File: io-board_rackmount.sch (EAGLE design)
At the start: 25 parts

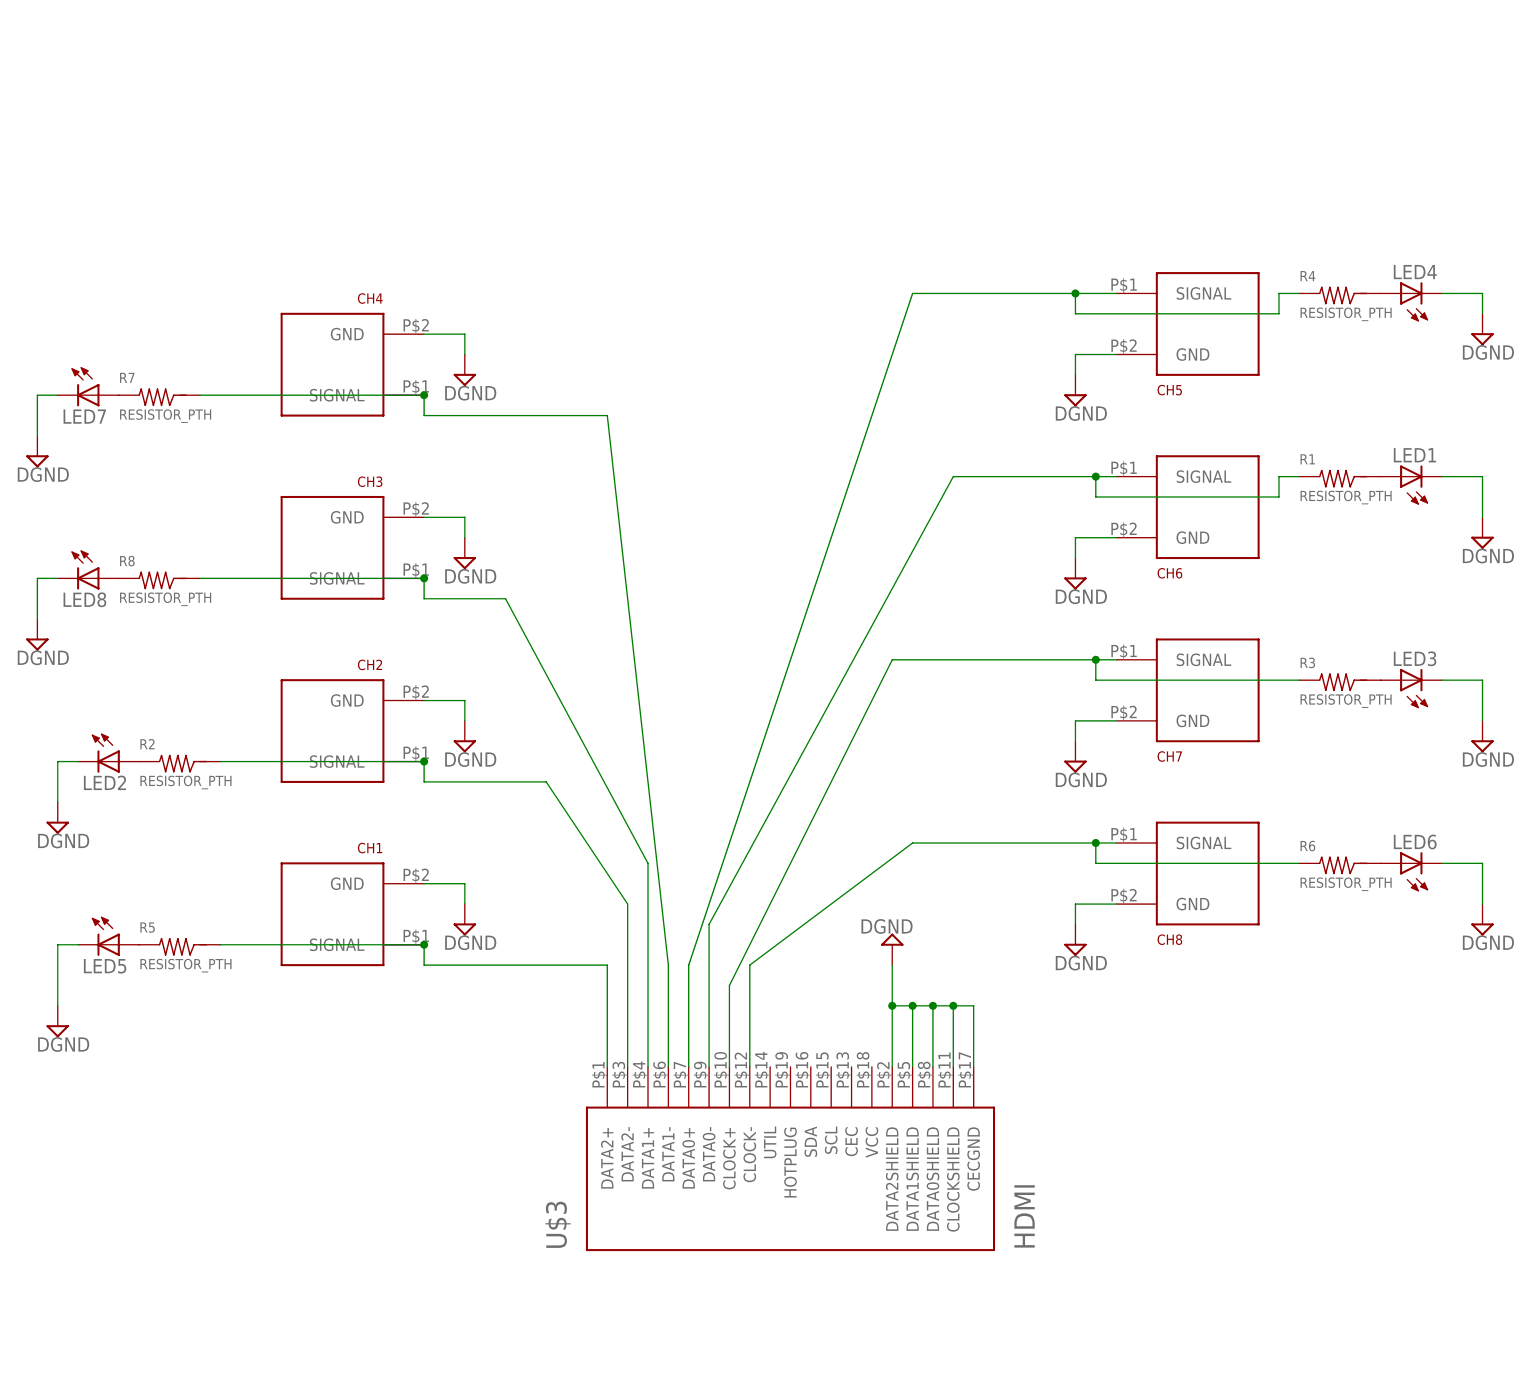
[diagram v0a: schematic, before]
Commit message: changed rackmounted IO board to single 8ch board
to be used with laser-cut mounting panel, or on its own
added pin headers for i2c and channels
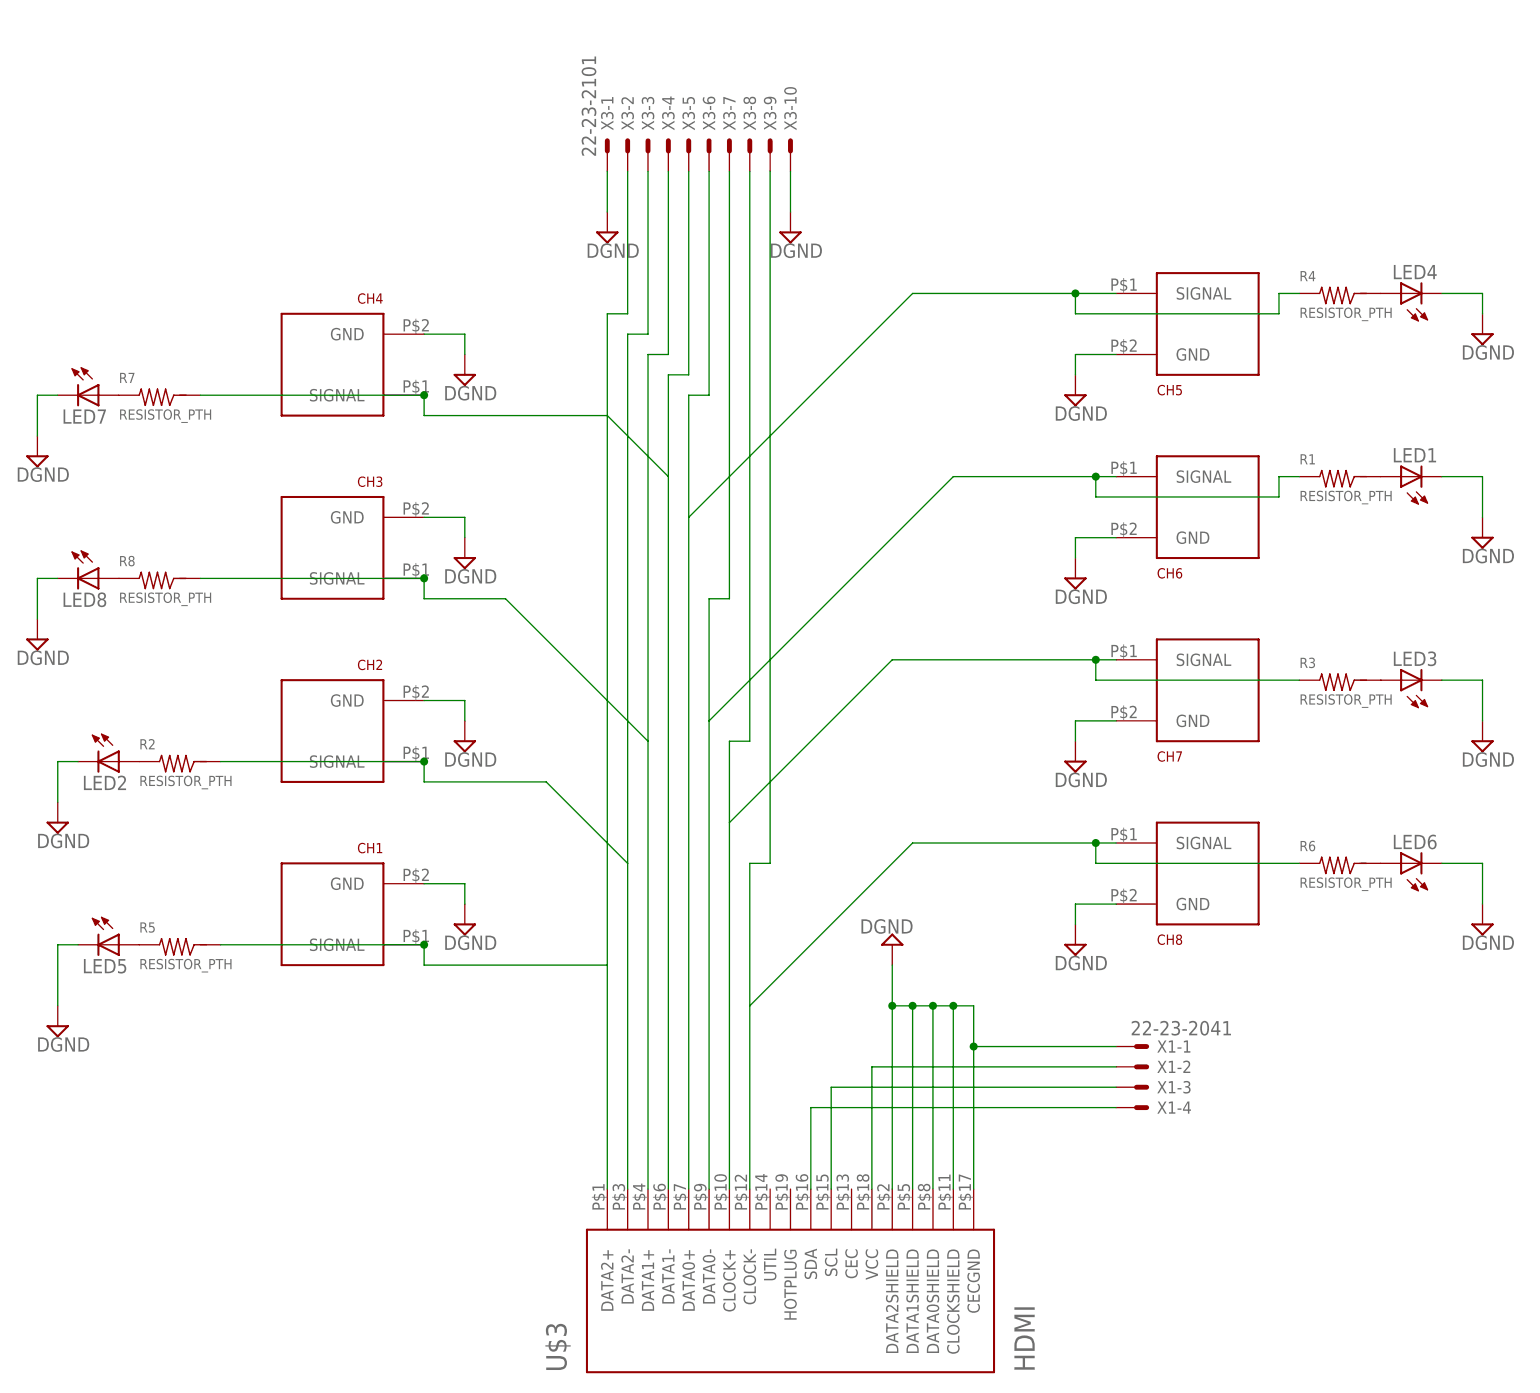
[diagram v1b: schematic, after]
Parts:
- added X1: 22-23-2041, con-molex:22-23-2041
- added X3: 22-23-2101, con-molex:22-23-2101
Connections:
- new net I2C_CLK: U$3.SCL, X1-3.S
- new net I2C_DAT: U$3.SDA, X1-4.S
- new net VCC: U$3.VCC, X1-2.S
- net CH6: now also X3-7.S
- net DGND: now also X1-1.S, X3-1.S, X3-10.S
- net N$2: now also X3-4.S
- net N$23: now also X3-5.S
- net N$3: now also X3-3.S
- net N$4: now also X3-2.S
- net N$5: now also X3-6.S
- net N$7: now also X3-8.S
- net N$8: now also X3-9.S
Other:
- moved on the sheet: U$3

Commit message: Remove LEDs
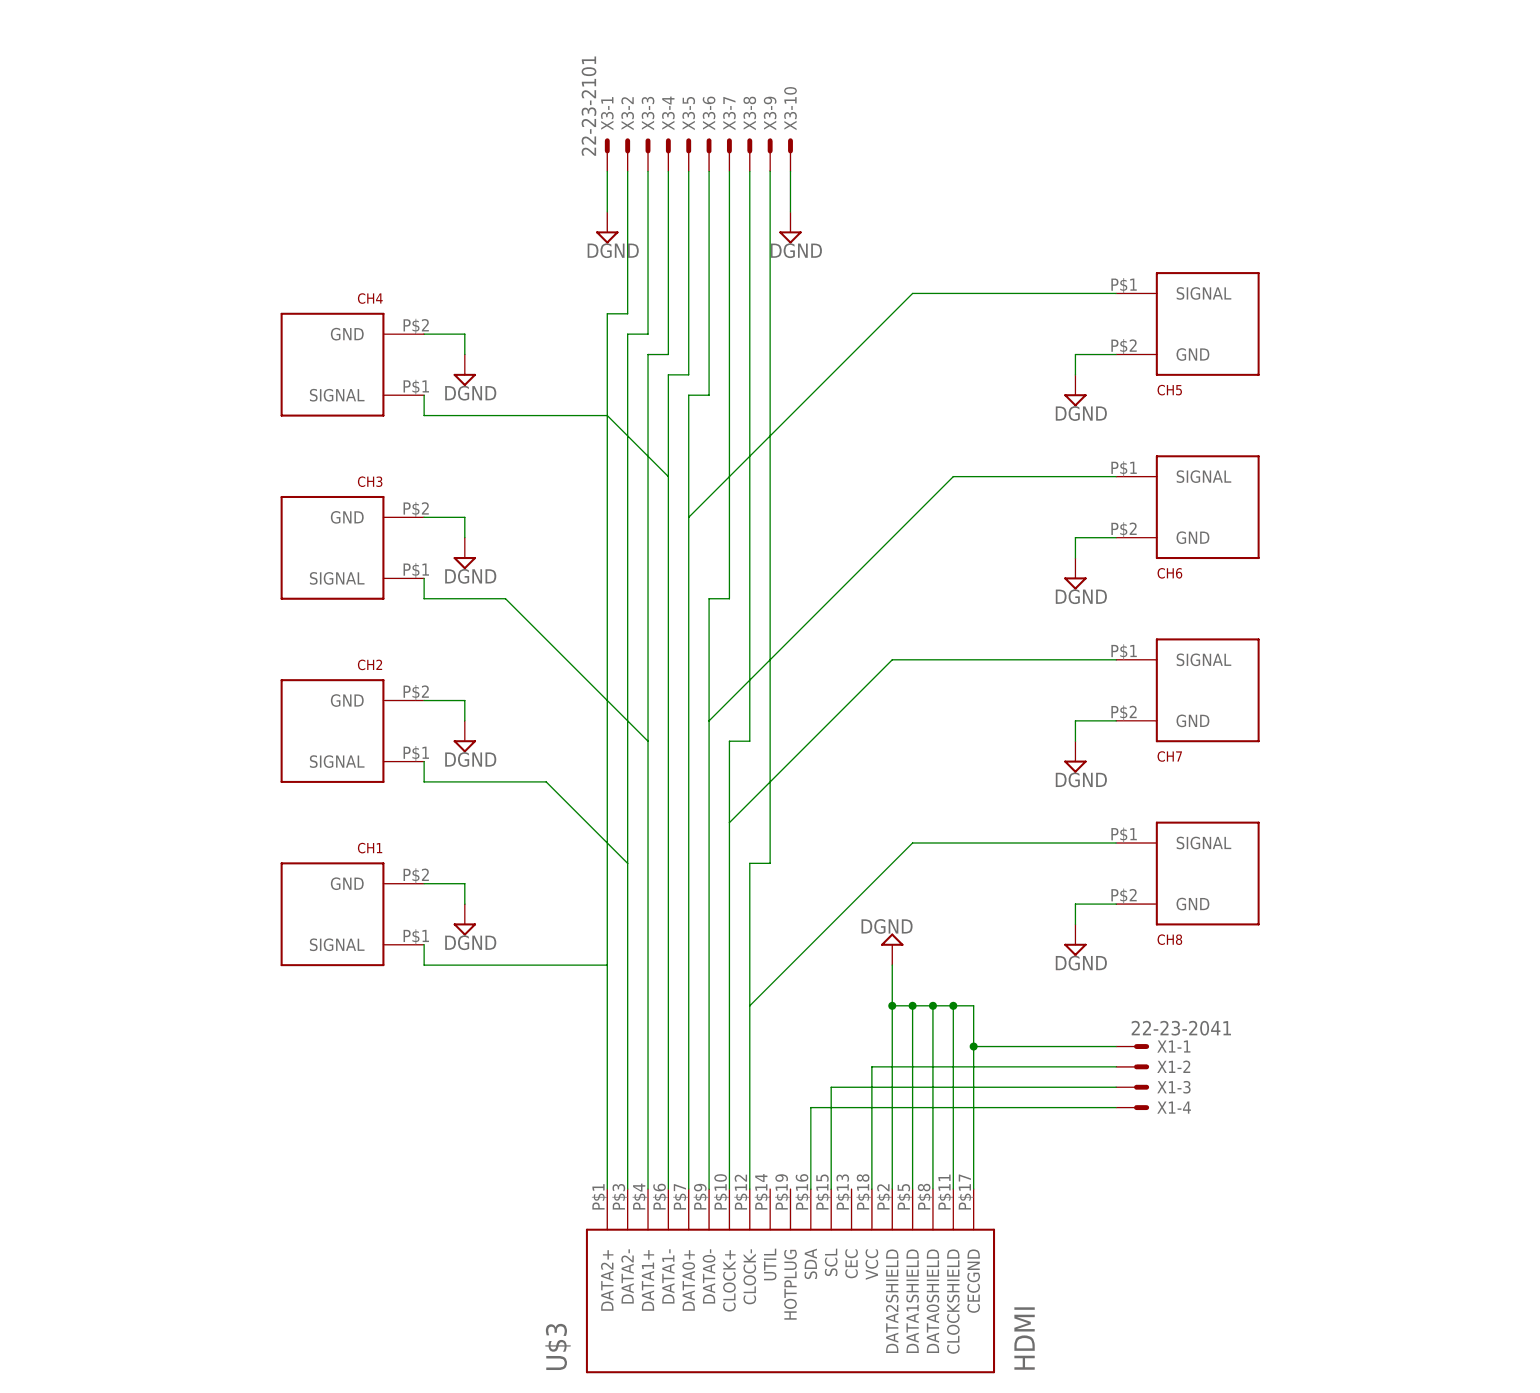
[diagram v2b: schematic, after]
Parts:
- removed LED1, LED2, LED3, LED4, LED5, LED6, LED7, LED8: (no value), sparkfun:LED3MM
- removed R1, R2, R3, R4, R5, R6, R7, R8: RESISTOR_PTH, josh:RESISTOR_PTH
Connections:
- removed net N$1: LED6.A, R6.P$2
- removed net N$10: LED1.A, R1.P$2
- removed net N$11: LED4.A, R4.P$2
- removed net N$12: LED7.A, R7.P$1
- removed net N$13: LED8.A, R8.P$1
- removed net N$14: LED2.A, R2.P$1
- removed net N$15: LED5.A, R5.P$1
- removed net N$9: LED3.A, R3.P$2
- net CH6: no longer R1.P$1
- net DGND: no longer LED1.C, LED2.C, LED3.C, LED4.C, LED5.C, LED6.C, LED7.C, LED8.C
- net N$2: no longer R8.P$2
- net N$23: no longer R7.P$2
- net N$3: no longer R2.P$2
- net N$4: no longer R5.P$2
- net N$5: no longer R4.P$1
- net N$7: no longer R3.P$1
- net N$8: no longer R6.P$1
